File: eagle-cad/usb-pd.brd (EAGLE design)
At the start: 68.6 x 53.3 mm, 49 parts, among them Q1 CERAMIC_RESONATOR_SMD6M00G53Z, T1 FDN360P, U1 ATMEGA328-AU

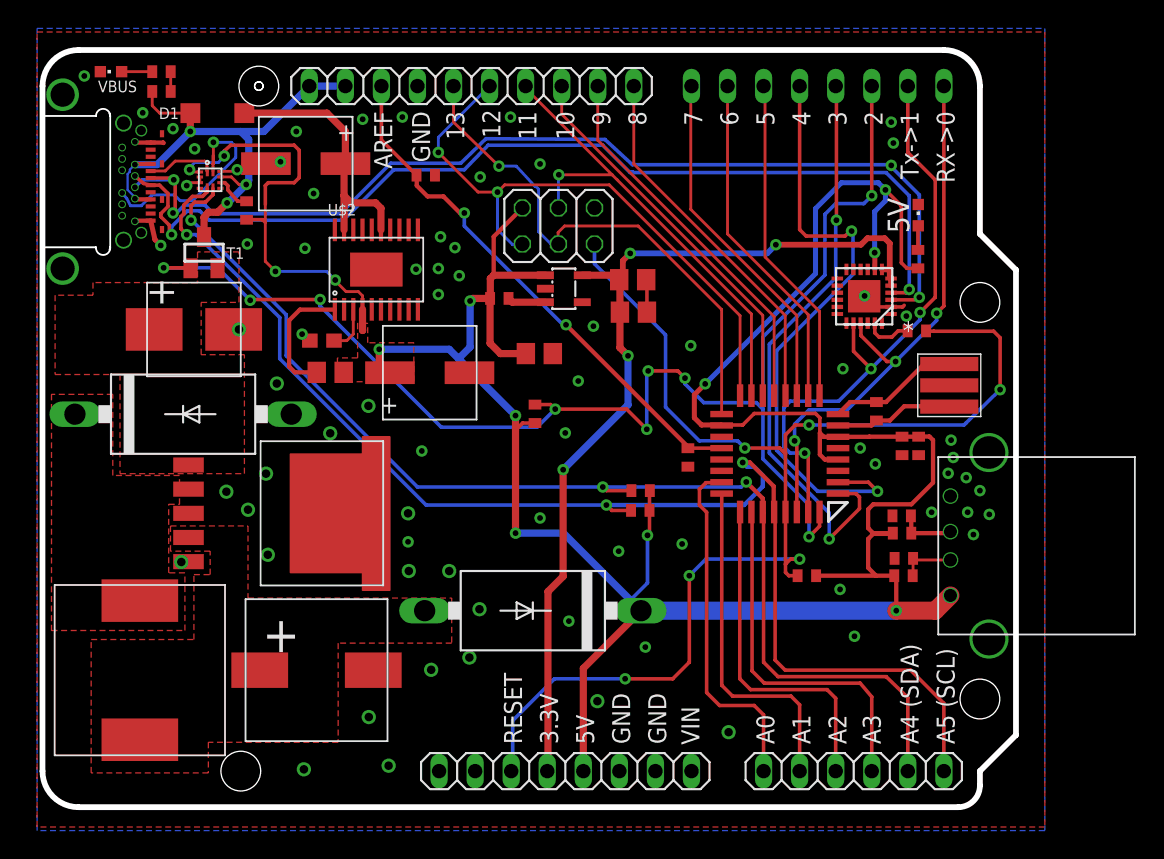
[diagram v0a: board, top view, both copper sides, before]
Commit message: Pushed DRC down to only 17 errors (from 550)
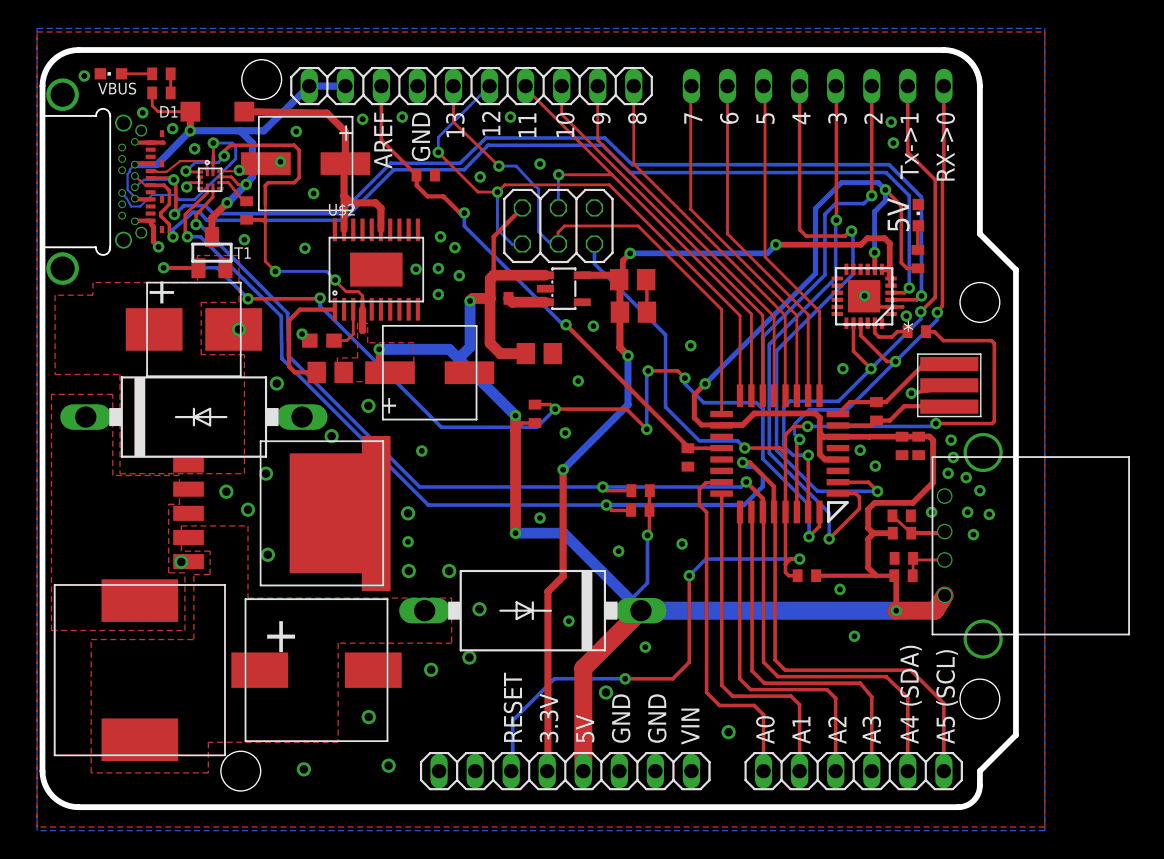
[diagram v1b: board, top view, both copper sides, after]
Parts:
- moved D2 0.79 mm to (10.7, 27.5)
- moved T1 0.56 mm to (11.9, 39.1)
- moved U$9 0.41 mm to (66.3, 18.4)
- moved R9 0.15 mm to (8.38, 51.7)
- moved VBUS 0.15 mm to (4.83, 51.7)
- moved D1 0.10 mm to (12.3, 49.0)
- moved R8 0.10 mm to (8.38, 50.3)
- moved C7 0.05 mm to (61.6, 33.5)
- turned R14 to 0 degrees
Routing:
- net GND: track 17.3 -> 22.1 mm
- net N$18: track 4.04 -> 4.77 mm
- net PD_SDA: track 83.8 -> 83.1 mm
- net IO2: track 96.6 -> 97.3 mm
- net PD_SCL: track 92.9 -> 92.3 mm

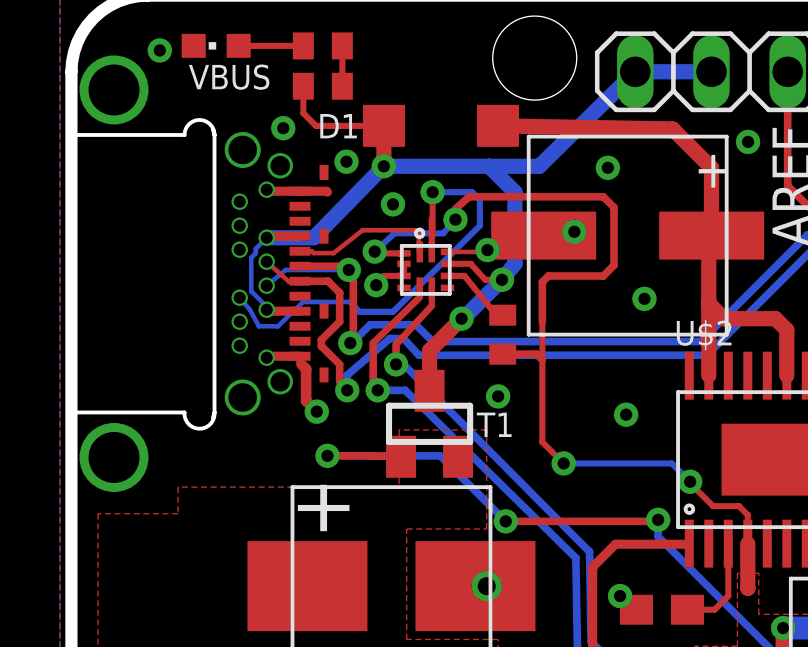
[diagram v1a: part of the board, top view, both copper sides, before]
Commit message: Fix disconnected ground plane
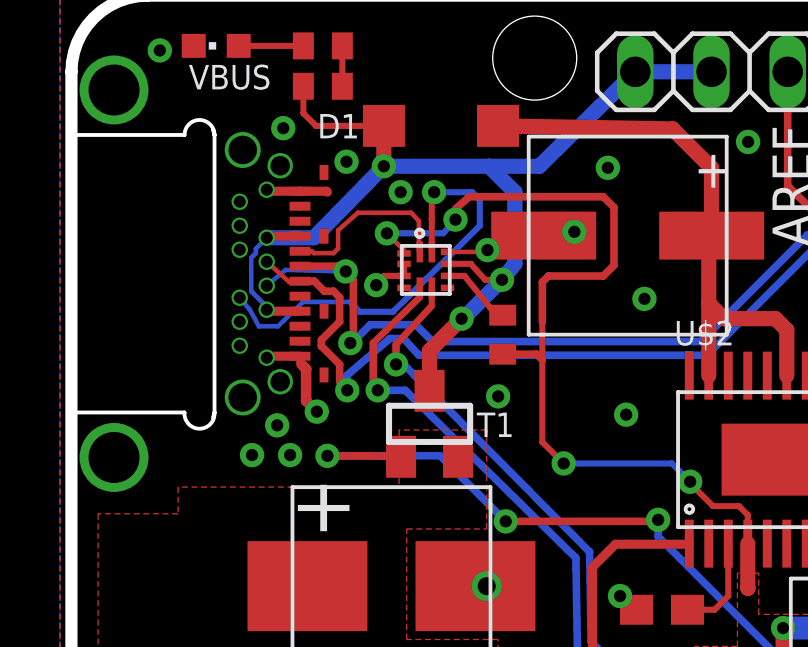
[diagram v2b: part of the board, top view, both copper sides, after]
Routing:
- net N$5: track 4.90 -> 6.04 mm
- net +5V: track 215.3 -> 214.6 mm
- net N$6: track 15.3 -> 14.7 mm
- net GND: vias 74 -> 77
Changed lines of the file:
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@@
 <setting verticaltext="up"/>
 </settings>
-<grid distance="2" unitdist="mil" unit="mil" style="lines" multiple="1" display="yes" altdistance="0.025" altunitdist="inch" altunit="inch"/>
+<grid distance="1" unitdist="mil" unit="mil" style="lines" multiple="1" display="yes" altdistance="0.025" altunitdist="inch" altunit="inch"/>
 <layers>
 <layer number="1" name="Top" color="4" fill="1" visible="yes" active="yes"/>
@@
 <wire x1="23.7236" y1="32.258" x2="23.7236" y2="31.363" width="0.508" layer="1"/>
 <wire x1="23.7236" y1="31.363" x2="24.4796" y2="30.607" width="0.508" layer="1"/>
-<wire x1="11.086" y1="44.746" x2="10.2196" y2="44.746" width="0.2032" layer="1"/>
-<wire x1="10.2196" y1="44.746" x2="10.1092" y2="44.8056" width="0.2032" layer="1"/>
-<via x="10.1092" y="44.8056" extent="1-16" drill="0.4064"/>
+<via x="10.5156" y="45.4152" extent="1-16" drill="0.4064"/>
 <wire x1="15.6972" y1="42.4688" x2="15.6972" y2="41.1988" width="0.2032" layer="1"/>
 <wire x1="15.6972" y1="41.1988" x2="15.6972" y2="38.4556" width="0.2032" layer="1"/>
@@
 <wire x1="58.5216" y1="19.304" x2="58.166" y2="19.6596" width="0.4064" layer="1"/>
 <wire x1="58.166" y1="19.6596" x2="58.166" y2="20.9804" width="0.4064" layer="1"/>
-<wire x1="10.1092" y1="44.8056" x2="10.7696" y2="45.4152" width="0.2032" layer="16"/>
-<wire x1="10.7696" y1="45.4152" x2="12.3952" y2="45.4152" width="0.2032" layer="16"/>
+<wire x1="10.5156" y1="45.4152" x2="12.3952" y2="45.4152" width="0.2032" layer="16"/>
 <wire x1="12.3952" y1="45.4152" x2="12.8016" y2="45.8724" width="0.2032" layer="16"/>
 <via x="12.8016" y="45.8724" extent="1-16" drill="0.4064"/>
@@
 <wire x1="31.7856" y1="37.4752" x2="31.7856" y2="40.193" width="0.3048" layer="1"/>
 <wire x1="31.7856" y1="40.193" x2="33.8074" y2="42.2148" width="0.3048" layer="1"/>
+<wire x1="11.086" y1="44.746" x2="11.086" y2="44.8448" width="0.1524" layer="1"/>
+<wire x1="11.086" y1="44.8448" x2="10.5156" y2="45.4152" width="0.1524" layer="1"/>
 </signal>
 <signal name="GND">
@@
 <wire x1="12.536" y1="44.796" x2="15.199" y2="44.796" width="0.1524" layer="1"/>
 <wire x1="15.199" y1="44.796" x2="15.742" y2="45.339" width="0.2032" layer="1"/>
-<via x="10.7188" y="46.3804" extent="1-16" drill="0.4064"/>
+<via x="10.9728" y="46.7868" extent="1-16" drill="0.4064"/>
 <via x="64.008" y="25.8572" extent="1-16" drill="0.4064"/>
 <via x="56.388" y="30.8864" extent="1-16" drill="0.4064"/>
@@
 <wire x1="7.8232" y1="40.894" x2="7.8232" y2="39.8272" width="0.3556" layer="1"/>
 <wire x1="7.8232" y1="39.8272" x2="8.1788" y2="39.4716" width="0.3556" layer="1"/>
-<wire x1="11.086" y1="44.396" x2="12.536" y2="44.796" width="0" layer="19" extent="1-1"/>
+<via x="7.2898" y="38.0238" extent="1-16" drill="0.4064"/>
+<via x="6.858" y="39.0144" extent="1-16" drill="0.4064"/>
+<via x="6.0198" y="38.0238" extent="1-16" drill="0.4064"/>
 </signal>
 <signal name="AREF">
@@
 <contactref element="U$3" pad="P$1"/>
 <contactref element="U$1" pad="A$5"/>
-<wire x1="11.43" y1="45.5168" x2="11.5824" y2="45.3644" width="0.1524" layer="1"/>
-<wire x1="11.5824" y1="45.3644" x2="11.5824" y2="44.8246" width="0.1524" layer="1"/>
 <wire x1="11.5824" y1="44.8246" x2="11.611" y2="44.796" width="0.1524" layer="1"/>
 <wire x1="7.62" y1="44.819" x2="8.013" y2="44.819" width="0.1524" layer="1"/>
 <wire x1="8.013" y1="44.819" x2="8.0772" y2="44.7548" width="0.1524" layer="1"/>
 <wire x1="8.0772" y1="44.7548" x2="8.7376" y2="44.7548" width="0.1524" layer="1"/>
-<wire x1="8.7376" y1="44.7548" x2="9.7028" y2="45.5168" width="0.1524" layer="1"/>
-<wire x1="9.7028" y1="45.5168" x2="11.43" y2="45.5168" width="0.1524" layer="1"/>
+<wire x1="8.7376" y1="44.7548" x2="8.89" y2="44.9072" width="0.1524" layer="1"/>
+<wire x1="8.89" y1="44.9072" x2="8.89" y2="45.5168" width="0.1524" layer="1"/>
+<wire x1="11.3284" y1="46.101" x2="11.5824" y2="45.8216" width="0.1524" layer="1"/>
+<wire x1="11.5824" y1="45.8216" x2="11.5824" y2="44.8246" width="0.1524" layer="1"/>
+<wire x1="11.3284" y1="46.101" x2="9.5504" y2="46.101" width="0.1524" layer="1"/>
+<wire x1="9.5504" y1="46.101" x2="8.89" y2="45.5168" width="0.1524" layer="1"/>
 </signal>
 <signal name="N$6">
 <contactref element="U$3" pad="P$2"/>
 <contactref element="U$1" pad="B$5"/>
-<wire x1="12.011" y1="44.796" x2="12.011" y2="45.3136" width="0.2032" layer="1"/>
-<wire x1="12.011" y1="45.3136" x2="12.011" y2="45.901" width="0.2032" layer="1"/>
+<wire x1="12.011" y1="44.796" x2="12.011" y2="45.8978" width="0.2032" layer="1"/>
+<wire x1="12.011" y1="45.8978" x2="12.011" y2="45.901" width="0.2032" layer="1"/>
 <wire x1="6.2484" y1="42.3164" x2="5.9436" y2="42.8752" width="0.1524" layer="16"/>
 <wire x1="5.9436" y1="42.8752" x2="5.61" y2="43.269" width="0.1524" layer="16"/>
@@
 <wire x1="13.6144" y1="45.6692" x2="13.6144" y2="46.5328" width="0.2032" layer="16"/>
 <wire x1="13.6144" y1="46.5328" x2="13.3604" y2="46.7868" width="0.2032" layer="16"/>
-<wire x1="13.3604" y1="46.7868" x2="12.0396" y2="46.7868" width="0.2032" layer="16"/>
-<via x="12.0396" y="46.7868" extent="1-16" drill="0.4064"/>
-<wire x1="12.0396" y1="46.7868" x2="12.0396" y2="45.3422" width="0.2032" layer="1"/>
-<wire x1="12.0396" y1="45.3422" x2="12.011" y2="45.3136" width="0.2032" layer="1"/>
+<wire x1="13.3604" y1="46.7868" x2="12.0904" y2="46.7868" width="0.2032" layer="16"/>
+<via x="12.0904" y="46.7868" extent="1-16" drill="0.4064"/>
+<wire x1="12.0904" y1="46.7868" x2="12.0142" y2="46.6884" width="0.2032" layer="1"/>
+<wire x1="12.0142" y1="46.6884" x2="12.011" y2="45.8978" width="0.2032" layer="1"/>
 <wire x1="7.7216" y1="43.1292" x2="9.2964" y2="43.1292" width="0.1524" layer="16"/>
 <wire x1="9.2964" y1="43.1292" x2="9.6012" y2="42.799" width="0.2032" layer="16"/>
@@
 <wire x1="29.718" y1="44.9072" x2="24.7396" y2="44.9072" width="0.254" layer="16"/>
 <wire x1="6.51" y1="44.469" x2="7.2644" y2="43.7896" width="0.1524" layer="1"/>
-<wire x1="7.62" y1="43.819" x2="8.5558" y2="43.819" width="0.254" layer="1"/>
-<wire x1="8.9408" y1="43.434" x2="8.9408" y2="42.4688" width="0.254" layer="1"/>
+<wire x1="8.9408" y1="43.2816" x2="8.9408" y2="42.4688" width="0.254" layer="1"/>
 <wire x1="21.1836" y1="41.3512" x2="24.7396" y2="44.9072" width="0.254" layer="16"/>
 <wire x1="8.9408" y1="41.0464" x2="8.9408" y2="40.4876" width="0.254" layer="1"/>
@@
 <wire x1="8.9408" y1="41.0464" x2="8.3312" y2="41.656" width="0.254" layer="1"/>
 <wire x1="8.3312" y1="41.656" x2="8.3312" y2="41.8592" width="0.254" layer="1"/>
-<wire x1="8.5558" y1="43.819" x2="8.9408" y2="43.434" width="0.254" layer="1"/>
 <wire x1="7.62" y1="43.819" x2="7.5906" y2="43.7896" width="0.2032" layer="1"/>
 <wire x1="7.5906" y1="43.7896" x2="7.2644" y2="43.7896" width="0.1524" layer="1"/>
+<wire x1="7.62" y1="43.819" x2="8.0986" y2="43.819" width="0.254" layer="1"/>
+<wire x1="8.0986" y1="43.819" x2="8.4328" y2="43.4848" width="0.254" layer="1"/>
+<wire x1="8.4328" y1="43.4848" x2="8.7376" y2="43.4848" width="0.254" layer="1"/>
+<wire x1="8.7376" y1="43.4848" x2="8.9408" y2="43.2816" width="0.254" layer="1"/>
 </signal>
 <signal name="+3V3">
@@
 <wire x1="31.242" y1="47.1424" x2="29.4132" y2="45.3644" width="0.254" layer="16"/>
 <wire x1="29.4132" y1="45.3644" x2="24.5364" y2="45.3644" width="0.254" layer="16"/>
-<wire x1="7.62" y1="44.319" x2="9.0718" y2="44.319" width="0.254" layer="1"/>
-<wire x1="9.0718" y1="44.319" x2="9.2456" y2="44.196" width="0.254" layer="1"/>
-<via x="9.2456" y="44.196" extent="1-16" drill="0.4064"/>
-<wire x1="9.2456" y1="44.196" x2="7.1386" y2="44.196" width="0.1524" layer="16"/>
+<wire x1="7.62" y1="44.319" x2="8.8686" y2="44.319" width="0.254" layer="1"/>
+<wire x1="8.8686" y1="44.319" x2="9.144" y2="44.1452" width="0.254" layer="1"/>
+<via x="9.144" y="44.1452" extent="1-16" drill="0.4064"/>
+<wire x1="9.144" y1="44.1452" x2="7.1386" y2="44.196" width="0.1524" layer="16"/>
 <wire x1="7.1386" y1="44.196" x2="6.51" y2="43.669" width="0.1524" layer="16"/>
-<wire x1="9.2456" y1="44.196" x2="9.398" y2="44.0436" width="0.254" layer="1"/>
-<wire x1="9.398" y1="44.0436" x2="9.398" y2="42.0624" width="0.254" layer="1"/>
+<wire x1="9.144" y1="44.1452" x2="9.398" y2="43.8404" width="0.254" layer="1"/>
+<wire x1="9.398" y1="43.8404" x2="9.398" y2="42.0624" width="0.254" layer="1"/>
 <wire x1="9.398" y1="42.0624" x2="9.2964" y2="41.7576" width="0.254" layer="1"/>
 <via x="9.2964" y="41.7576" extent="1-16" drill="0.4064"/>
